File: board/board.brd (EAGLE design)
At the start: 94 x 44.5 mm, 115 parts, among them IC1 STM32F05XC, IC2 MCP6N11-10, IC3 MCP45X1, IC4 LD117ADT33TR, IC5 FT230XS, IC6 MCP6002, IC7 LIS331, Q1 MMBT2222A, Q2 MMBT2222A, Q3 MMBT2222A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

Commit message: Adding Nil RTOS, changed value of digital pot to proper part name.
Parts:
- IC3: value MCP45X1 -> MCP4551-100K
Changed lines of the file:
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@@
 <attribute name="NAME" x="32.7025" y="1.5875" size="1.27" layer="26" font="vector" ratio="16" rot="MR180"/>
 </element>
-<element name="IC3" library="misc" package="MSOP-8" value="MCP45X1" x="44.45" y="4.445" smashed="yes" rot="MR180">
+<element name="IC3" library="misc" package="MSOP-8" value="MCP4551-100K" x="44.45" y="4.445" smashed="yes" rot="MR180">
 <attribute name="VALUE" x="43.35" y="5.045" size="0.4064" layer="28" rot="MR180"/>
 <attribute name="NAME" x="42.5975" y="1.405" size="1.27" layer="26" font="vector" ratio="16" rot="MR180"/>

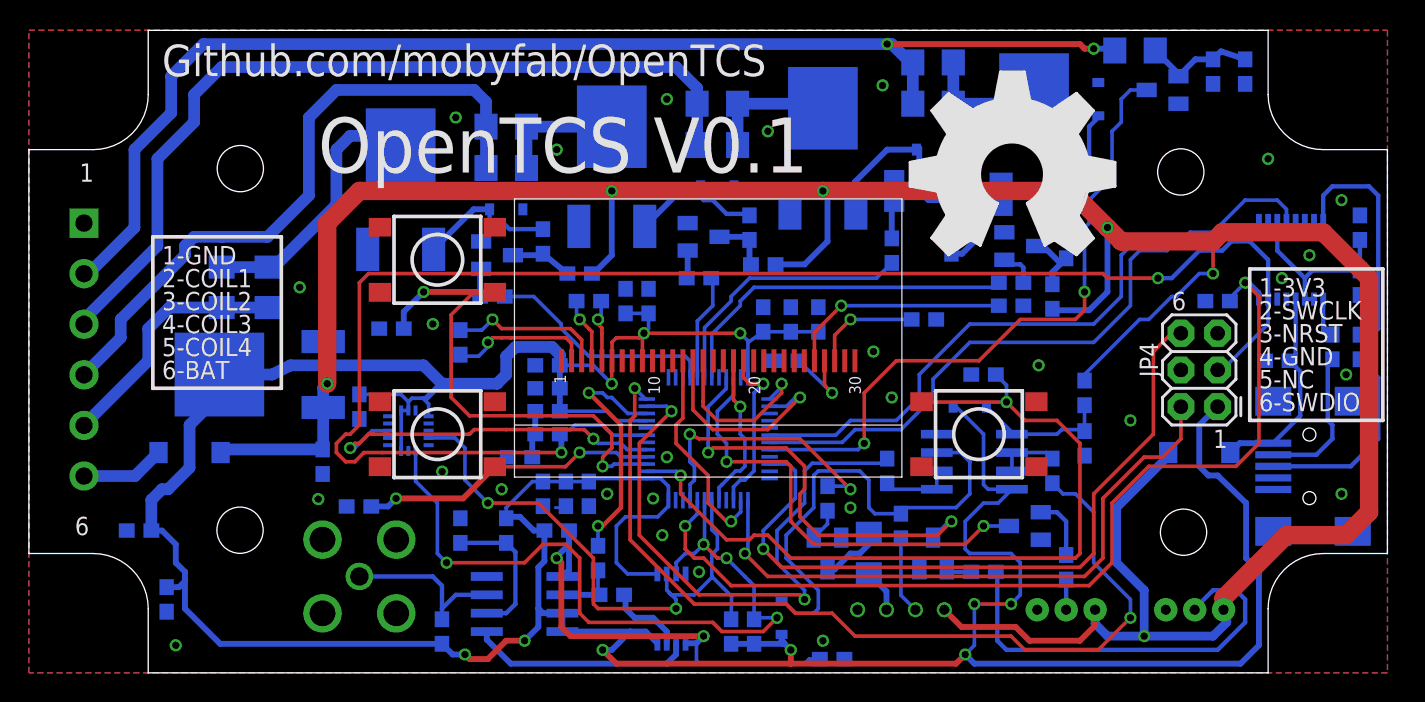
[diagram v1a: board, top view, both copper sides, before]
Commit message: Adding output for external fuel/igntion controller.
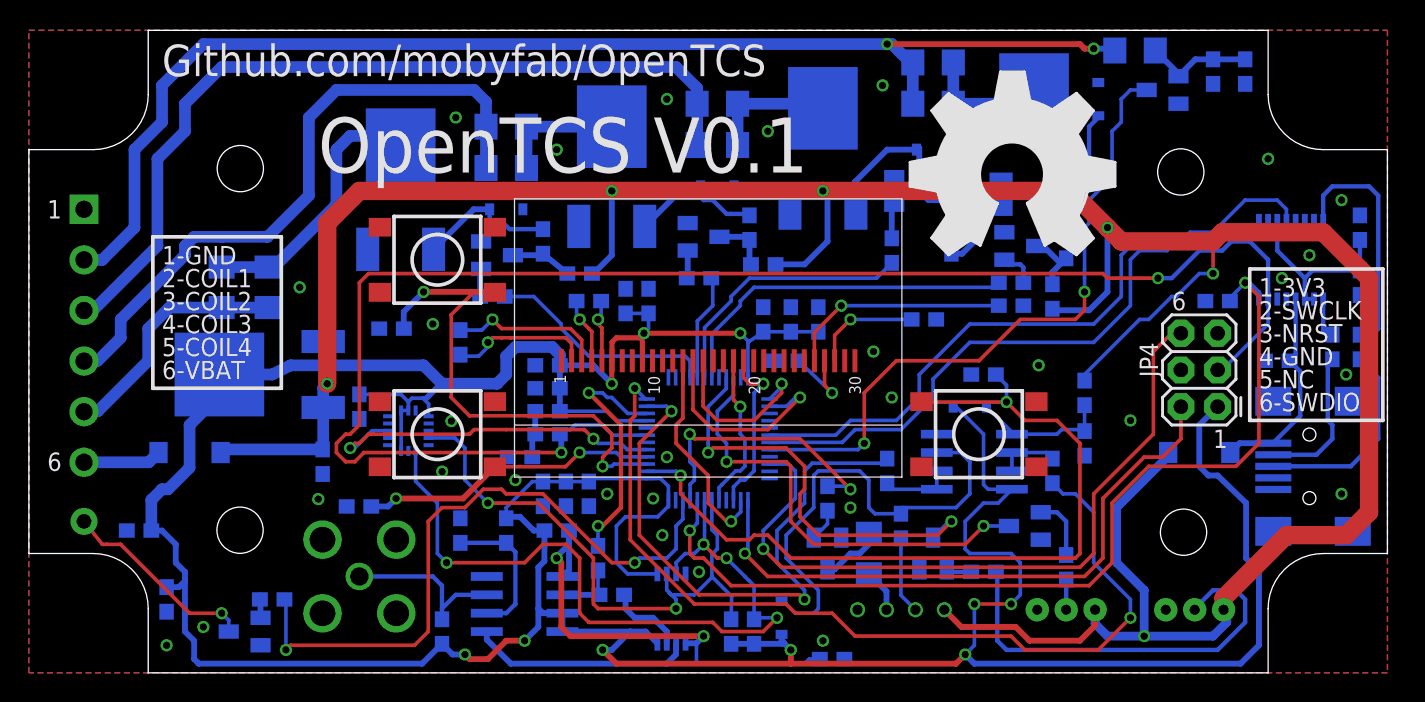
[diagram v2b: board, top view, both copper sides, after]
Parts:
- added JP5: M01PTH, SparkFun-Connectors:1X01
- added Q9: MMBT2222A, SparkFun-DiscreteSemi:SOT23
- added R39: 10K, SparkFun-Resistors:0603-RES
- moved JP6 0.95 mm to (3.81, 32.1)
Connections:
- new net CUT_OUT: JP5.1, Q9.3
- new net CUT_OUT_TRIG: IC1.46, R39.2
- new net N$37: Q9.1, R39.1
- net GND: now also Q9.2
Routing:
- net CUT_OUT_TRIG: track 0.00 -> 46.1 mm, vias 0 -> 2
- net CUT_OUT: track 0.00 -> 13.7 mm, vias 0 -> 1
- net +3V3: track 272.4 -> 275.2 mm
- net N$37: track 0.00 -> 1.82 mm
- net COIL2_IN: track 59.2 -> 58.6 mm
- net GND: vias 28 -> 30
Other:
- board text added: "6-VBAT"
- board text removed: "6-BAT"

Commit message: Changed connectors
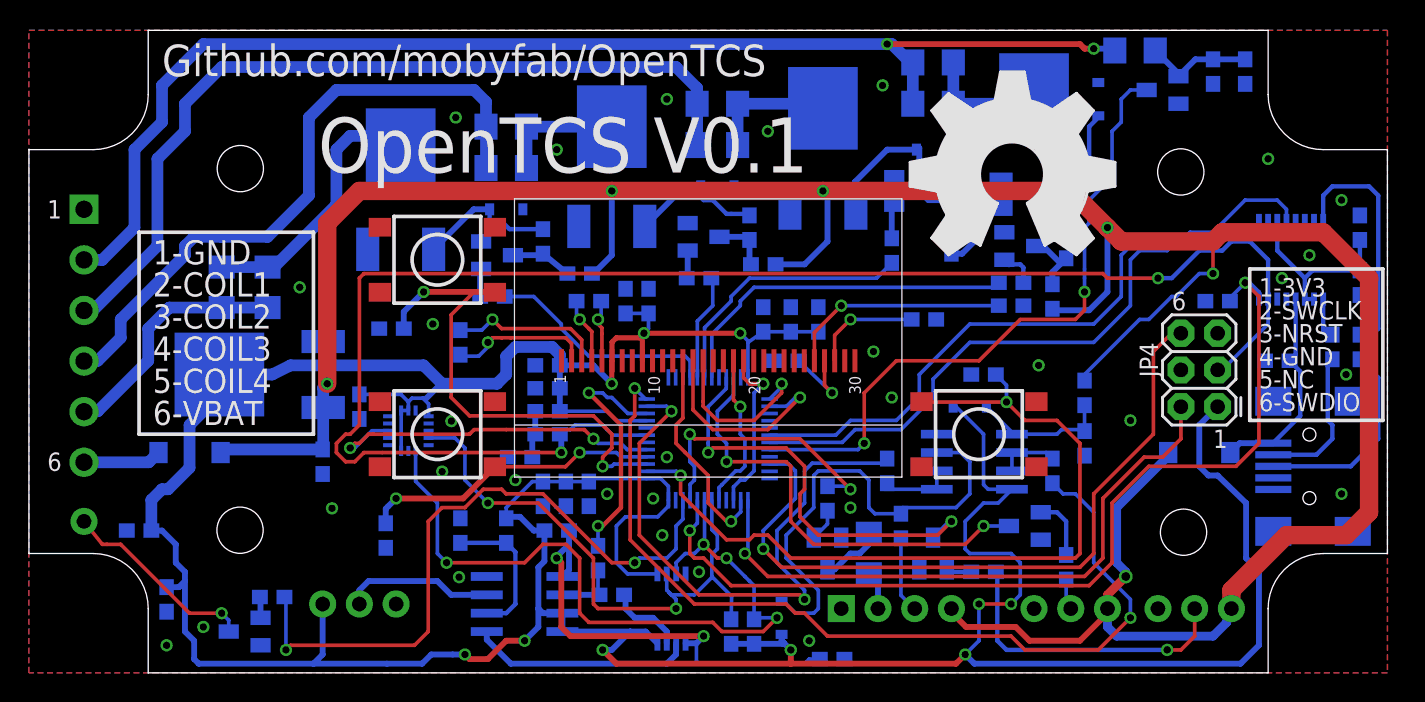
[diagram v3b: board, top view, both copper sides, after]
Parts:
- removed R12: 120R, SparkFun-Resistors:0603-RES
- removed X1: BU-SMA-G, con-coax:BU-SMA-G
- added JP8: (no value), SparkFun-Connectors:1X03
- JP2, JP3: device SparkFun-Connectors:JST-3-PTH -> SparkFun-Connectors:1X03
- JP7: device SparkFun-Connectors:JST-4-PTH -> SparkFun-Connectors:1X04
- moved JP7 6.55 mm to (56.2, 4.45)
- moved JP2 5.68 mm to (78.1, 4.45)
- moved JP3 5.54 mm to (69.5, 4.45)
- moved C22 2.74 mm to (24.7, 9.50), turned to 270 degrees
- moved R39 0.17 mm to (16.8, 5.25)
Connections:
- net +3V3: now also JP8.1; no longer R12.1
- net GND: now also JP8.3; no longer X1.2, X1.3, X1.4, X1.5
- net VIP: now also JP8.2; no longer R12.2, X1.1
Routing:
- net N$33: track 29.1 -> 21.0 mm, vias 0 -> 1
- net +3V3: track 275.2 -> 278.8 mm
- net VCC: track 211.3 -> 208.7 mm
- net VIP: track 11.8 -> 10.4 mm
- net GND: vias 30 -> 31
